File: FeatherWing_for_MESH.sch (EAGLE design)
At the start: 21 parts, among them J1 NF, J2 NF

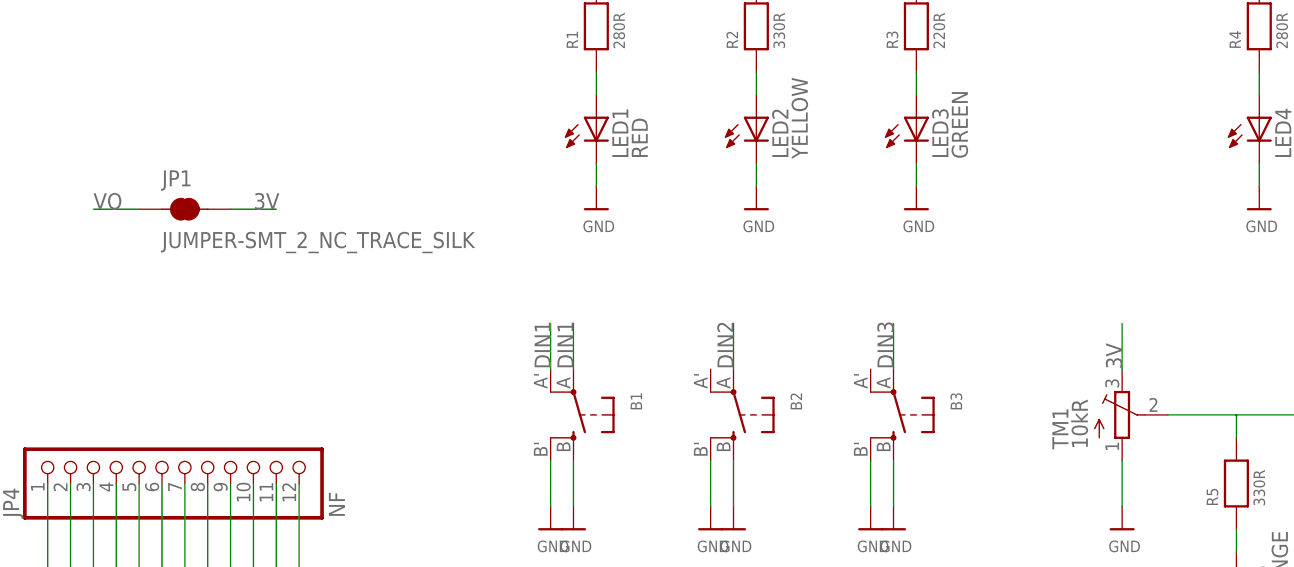
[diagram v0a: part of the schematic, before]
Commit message: v1.1 Add Mesh pin1 marking, move LEDs away from buttons, default not to connect 3V and Vout. Panelized garber.
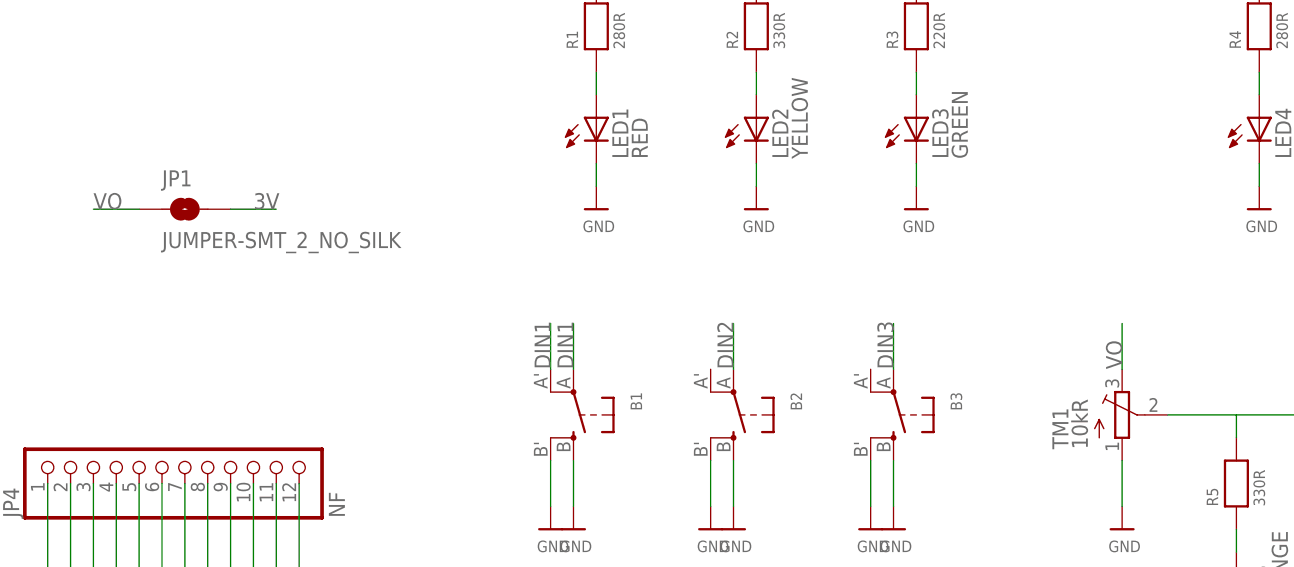
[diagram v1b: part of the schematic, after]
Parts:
- JP1: value JUMPER-SMT_2_NC_TRACE_SILK -> JUMPER-SMT_2_NO_SILK; device SparkFun-Jumpers:JUMPER-SMT_2_NC_TRACE_SILK -> SparkFun-Jumpers:JUMPER-SMT_2_NO_SILK
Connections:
- net 3V: no longer TM1.E
- net VO: now also TM1.E
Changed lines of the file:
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@@
 <?xml version="1.0" encoding="utf-8"?>
 <!DOCTYPE eagle SYSTEM "eagle.dtd">
-<eagle version="8.6.1">
+<eagle version="9.0.0">
 <drawing>
 <settings>
@@
 <part name="J2" library="SparkFun-Connectors" library_urn="urn:adsk.eagle:library:513" deviceset="CONN_05X2" device="NO_SILK" package3d_urn="urn:adsk.eagle:package:38114/1" value="NF"/>
 <part name="JP2" library="SparkFun-Jumpers" library_urn="urn:adsk.eagle:library:528" deviceset="JUMPER-SMT_3_1-NC_TRACE" device="_SILK" package3d_urn="urn:adsk.eagle:package:39288/1"/>
-<part name="JP1" library="SparkFun-Jumpers" library_urn="urn:adsk.eagle:library:528" deviceset="JUMPER-SMT_2_NC_TRACE" device="_SILK" package3d_urn="urn:adsk.eagle:package:39281/1"/>
+<part name="JP1" library="SparkFun-Jumpers" library_urn="urn:adsk.eagle:library:528" deviceset="JUMPER-SMT_2_NO" device="_SILK" package3d_urn="urn:adsk.eagle:package:39279/1"/>
 <part name="U$1" library="microbuilder" deviceset="GND" device=""/>
 <part name="U$11" library="microbuilder" deviceset="GND" device=""/>
@@
 <label x="114.3" y="132.08" size="1.778" layer="95"/>
 </segment>
+</net>
+<net name="N$18" class="0">
+<segment>
+<pinref part="MS1" gate="G$1" pin="!RESET"/>
+<pinref part="JP3" gate="A" pin="16"/>
+<wire x1="81.28" y1="22.86" x2="81.28" y2="40.64" width="0.1524" layer="91"/>
+</segment>
+</net>
+<net name="VBAT" class="0">
+<segment>
+<pinref part="MS1" gate="G$1" pin="VBAT"/>
+<pinref part="JP4" gate="G$1" pin="1"/>
+<wire x1="91.44" y1="101.6" x2="91.44" y2="83.82" width="0.1524" layer="91"/>
+</segment>
+</net>
+<net name="N$1" class="0">
+<segment>
+<pinref part="MS1" gate="G$1" pin="EN"/>
+<pinref part="JP4" gate="G$1" pin="2"/>
+<wire x1="93.98" y1="101.6" x2="93.98" y2="83.82" width="0.1524" layer="91"/>
+</segment>
+</net>
+<net name="USB" class="0">
+<segment>
+<pinref part="MS1" gate="G$1" pin="USB"/>
+<pinref part="JP4" gate="G$1" pin="3"/>
+<wire x1="96.52" y1="101.6" x2="96.52" y2="83.82" width="0.1524" layer="91"/>
+</segment>
+</net>
+<net name="N$21" class="0">
+<segment>
+<pinref part="MS1" gate="G$1" pin="GPIO9"/>
+<pinref part="JP4" gate="G$1" pin="8"/>
+<wire x1="109.22" y1="101.6" x2="109.22" y2="83.82" width="0.1524" layer="91"/>
+</segment>
+</net>
+<net name="N$24" class="0">
+<segment>
+<pinref part="MS1" gate="G$1" pin="GPIOSCL"/>
+<pinref part="JP4" gate="G$1" pin="11"/>
+<wire x1="116.84" y1="101.6" x2="116.84" y2="83.82" width="0.1524" layer="91"/>
+</segment>
+</net>
+<net name="N$25" class="0">
+<segment>
+<pinref part="MS1" gate="G$1" pin="GPIOSDA"/>
+<pinref part="JP4" gate="G$1" pin="12"/>
+<wire x1="119.38" y1="101.6" x2="119.38" y2="83.82" width="0.1524" layer="91"/>
+</segment>
+</net>
+<net name="N$16" class="0">
+<segment>
+<pinref part="LED1" gate="G$1" pin="A"/>
+<pinref part="R1" gate="G$1" pin="1"/>
+<wire x1="152.4" y1="144.78" x2="152.4" y2="147.32" width="0.1524" layer="91"/>
+</segment>
+</net>
+<net name="N$17" class="0">
+<segment>
+<pinref part="R2" gate="G$1" pin="1"/>
+<pinref part="LED2" gate="G$1" pin="A"/>
+<wire x1="170.18" y1="147.32" x2="170.18" y2="144.78" width="0.1524" layer="91"/>
+</segment>
+</net>
+<net name="N$26" class="0">
+<segment>
+<pinref part="R3" gate="G$1" pin="1"/>
+<pinref part="LED3" gate="G$1" pin="A"/>
+<wire x1="187.96" y1="147.32" x2="187.96" y2="144.78" width="0.1524" layer="91"/>
+</segment>
+</net>
+<net name="N$27" class="0">
+<segment>
+<pinref part="R4" gate="G$1" pin="1"/>
+<pinref part="LED4" gate="G$1" pin="A"/>
+<wire x1="226.06" y1="147.32" x2="226.06" y2="144.78" width="0.1524" layer="91"/>
+</segment>
+</net>
+<net name="VO" class="0">
+<segment>
+<pinref part="J1" gate="G$1" pin="1"/>
+<wire x1="45.72" y1="144.78" x2="35.56" y2="144.78" width="0.1524" layer="91"/>
+<label x="35.56" y="144.78" size="1.778" layer="95"/>
+</segment>
+<segment>
+<pinref part="J2" gate="G$1" pin="1"/>
+<wire x1="45.72" y1="121.92" x2="35.56" y2="121.92" width="0.1524" layer="91"/>
+<label x="35.56" y="121.92" size="1.778" layer="95"/>
+</segment>
+<segment>
+<pinref part="JP1" gate="G$1" pin="1"/>
+<wire x1="101.6" y1="132.08" x2="96.52" y2="132.08" width="0.1524" layer="91"/>
+<label x="96.52" y="132.08" size="1.778" layer="95"/>
+</segment>
 <segment>
 <pinref part="TM1" gate="G$1" pin="E"/>
@@
 </segment>
 </net>
-<net name="N$18" class="0">
-<segment>
-<pinref part="MS1" gate="G$1" pin="!RESET"/>
-<pinref part="JP3" gate="A" pin="16"/>
-<wire x1="81.28" y1="22.86" x2="81.28" y2="40.64" width="0.1524" layer="91"/>
-</segment>
-</net>
-<net name="VBAT" class="0">
-<segment>
-<pinref part="MS1" gate="G$1" pin="VBAT"/>
-<pinref part="JP4" gate="G$1" pin="1"/>
-<wire x1="91.44" y1="101.6" x2="91.44" y2="83.82" width="0.1524" layer="91"/>
-</segment>
-</net>
-<net name="N$1" class="0">
-<segment>
-<pinref part="MS1" gate="G$1" pin="EN"/>
-<pinref part="JP4" gate="G$1" pin="2"/>
-<wire x1="93.98" y1="101.6" x2="93.98" y2="83.82" width="0.1524" layer="91"/>
-</segment>
-</net>
-<net name="USB" class="0">
-<segment>
-<pinref part="MS1" gate="G$1" pin="USB"/>
-<pinref part="JP4" gate="G$1" pin="3"/>
-<wire x1="96.52" y1="101.6" x2="96.52" y2="83.82" width="0.1524" layer="91"/>
-</segment>
-</net>
-<net name="N$21" class="0">
-<segment>
-<pinref part="MS1" gate="G$1" pin="GPIO9"/>
-<pinref part="JP4" gate="G$1" pin="8"/>
-<wire x1="109.22" y1="101.6" x2="109.22" y2="83.82" width="0.1524" layer="91"/>
-</segment>
-</net>
-<net name="N$24" class="0">
-<segment>
-<pinref part="MS1" gate="G$1" pin="GPIOSCL"/>
-<pinref part="JP4" gate="G$1" pin="11"/>
-<wire x1="116.84" y1="101.6" x2="116.84" y2="83.82" width="0.1524" layer="91"/>
-</segment>
-</net>
-<net name="N$25" class="0">
-<segment>
-<pinref part="MS1" gate="G$1" pin="GPIOSDA"/>
-<pinref part="JP4" gate="G$1" pin="12"/>
-<wire x1="119.38" y1="101.6" x2="119.38" y2="83.82" width="0.1524" layer="91"/>
-</segment>
-</net>
-<net name="N$16" class="0">
-<segment>
-<pinref part="LED1" gate="G$1" pin="A"/>
-<pinref part="R1" gate="G$1" pin="1"/>
-<wire x1="152.4" y1="144.78" x2="152.4" y2="147.32" width="0.1524" layer="91"/>
-</segment>
-</net>
-<net name="N$17" class="0">
-<segment>
-<pinref part="R2" gate="G$1" pin="1"/>
-<pinref part="LED2" gate="G$1" pin="A"/>
-<wire x1="170.18" y1="147.32" x2="170.18" y2="144.78" width="0.1524" layer="91"/>
-</segment>
-</net>
-<net name="N$26" class="0">
-<segment>
-<pinref part="R3" gate="G$1" pin="1"/>
-<pinref part="LED3" gate="G$1" pin="A"/>
-<wire x1="187.96" y1="147.32" x2="187.96" y2="144.78" width="0.1524" layer="91"/>
-</segment>
-</net>
-<net name="N$27" class="0">
-<segment>
-<pinref part="R4" gate="G$1" pin="1"/>
-<pinref part="LED4" gate="G$1" pin="A"/>
-<wire x1="226.06" y1="147.32" x2="226.06" y2="144.78" width="0.1524" layer="91"/>
-</segment>
-</net>
-<net name="VO" class="0">
-<segment>
-<pinref part="J1" gate="G$1" pin="1"/>
-<wire x1="45.72" y1="144.78" x2="35.56" y2="144.78" width="0.1524" layer="91"/>
-<label x="35.56" y="144.78" size="1.778" layer="95"/>
-</segment>
-<segment>
-<pinref part="J2" gate="G$1" pin="1"/>
-<wire x1="45.72" y1="121.92" x2="35.56" y2="121.92" width="0.1524" layer="91"/>
-<label x="35.56" y="121.92" size="1.778" layer="95"/>
-</segment>
-<segment>
-<pinref part="JP1" gate="G$1" pin="1"/>
-<wire x1="101.6" y1="132.08" x2="96.52" y2="132.08" width="0.1524" layer="91"/>
-<label x="96.52" y="132.08" size="1.778" layer="95"/>
-</segment>
-</net>
